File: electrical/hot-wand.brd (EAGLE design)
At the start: 112 x 72 mm, 192 parts, among them IC1 12V R-78K12-2.0, IC2 3V3 R-78K3.3, Q1 STP19NF20, Q2 IRF510, Q3 BC846B, Q4 SIS862ADN-T1-GE3, Q5 2N7002K, Q6 DMTH64M2LPDWQ-13, Q7 SIS862ADN-T1-GE3, Q8 G3404, U1 TPS54560DDA, U2 1EDN8511BXUSA1, U3 INA138, U4 LM74700QDBVTQ1, U5 AP53781, U6 SSD1306-4PIN-0.91N-VERT, U7 STM32F030F4P6, Y1 27.12 MHz 10pF

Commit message: Update hot-wand.brd
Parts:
- moved LED1 19.3 mm to (24.0, 70.1), turned to 0 degrees
- moved R39 10.9 mm to (25.7, 64.8), turned to 0 degrees
- moved R38 8.33 mm to (29.0, 64.8)
- moved LED2 1.80 mm to (25.8, 43.3)
- moved C5 0.50 mm to (29.5, 61.5)
- moved R44 0.30 mm to (20.7, 16.0)
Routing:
- net N$46: track 2.35 -> 4.90 mm
- net N$47: track 4.10 -> 2.30 mm
- net N$35: track 23.8 -> 24.9 mm
- net N$44: track 20.8 -> 21.7 mm
- net GND: vias 657 -> 655

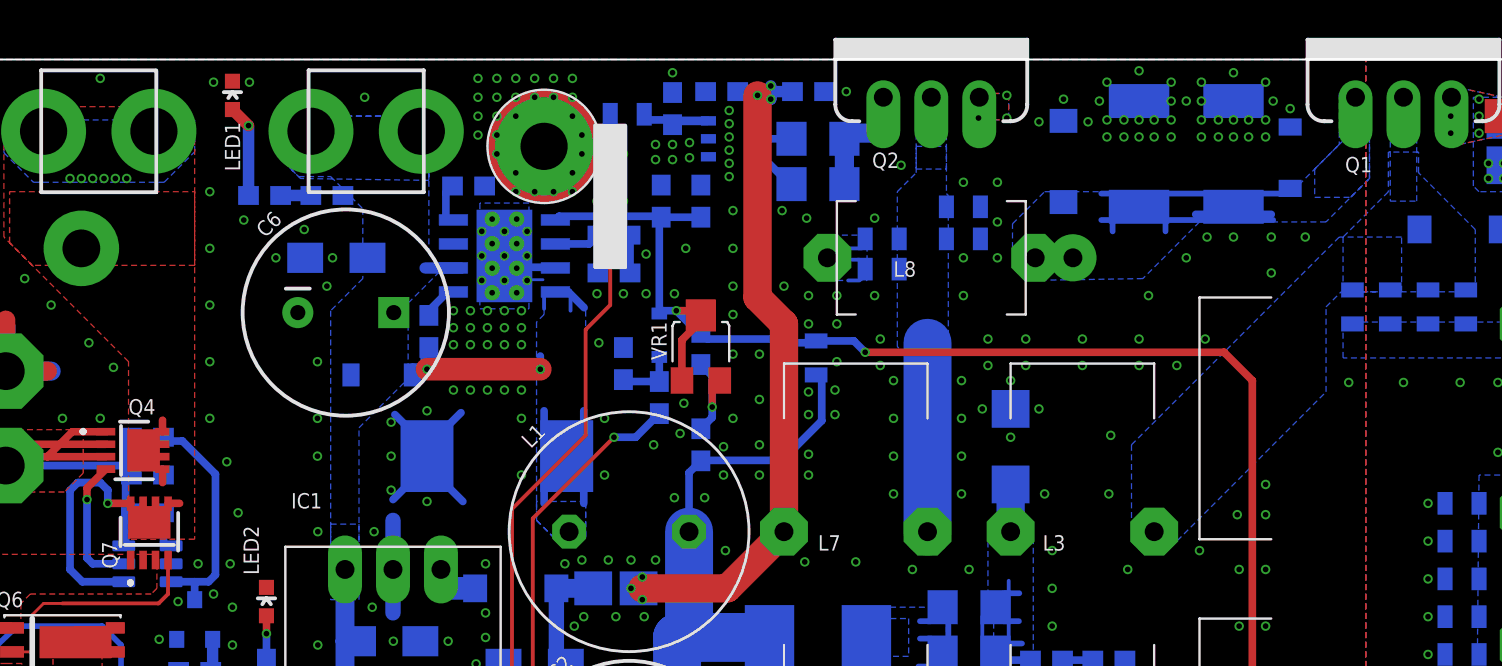
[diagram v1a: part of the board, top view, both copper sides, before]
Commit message: brd change, option for larger TH resistors over SMD ones
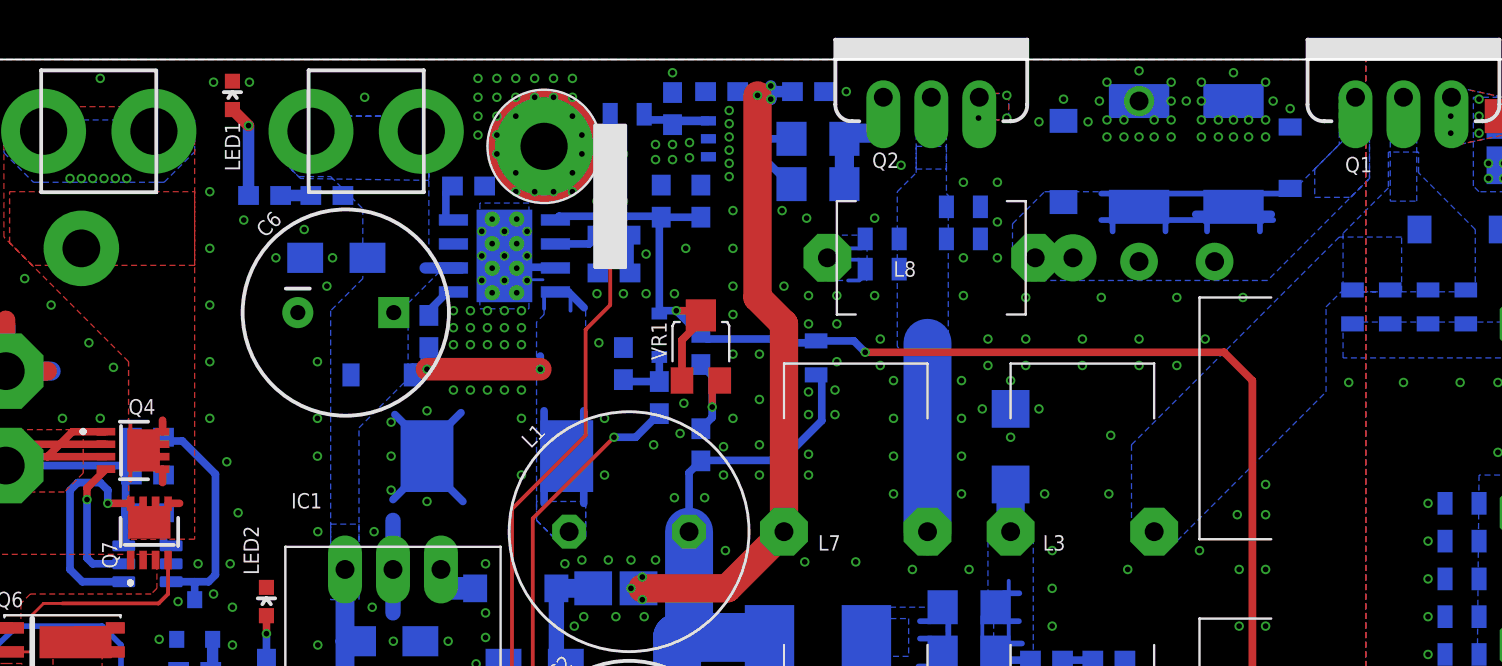
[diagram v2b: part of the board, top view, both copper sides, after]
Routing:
- net DC-SRC: track 13.5 -> 16.6 mm
- net RF-GATE: track 23.7 -> 24.7 mm, vias 1 -> 3
- net GND: vias 655 -> 652
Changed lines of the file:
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@@
 </element>
 <element name="D9" library="hot-wand" package="SOD123FL" value="STPS0540Z" x="80" y="66.8" smashed="yes" rot="MR90">
-<attribute name="NAME" x="80.316" y="69.211" size="0.8128" layer="26" font="vector" rot="MR90"/>
+<attribute name="NAME" x="80.416" y="69.311" size="0.8128" layer="26" font="vector" rot="MR90"/>
 <attribute name="JLCPARTNUM" value="C181835" x="80" y="66.8" size="1.778" layer="28" rot="MR90" display="off"/>
 </element>
 <element name="R13" library="hot-wand" package="R2512" value="DNP" x="72" y="67" smashed="yes" rot="MR270">
-<attribute name="NAME" x="70.16" y="62.795" size="0.8128" layer="26" font="vector" rot="MR180"/>
-<attribute name="VALUE" x="70.16" y="61.775" size="0.8128" layer="28" font="vector" rot="MR180"/>
+<attribute name="NAME" x="70.26" y="67.395" size="0.8128" layer="26" font="vector" rot="MR180"/>
+<attribute name="VALUE" x="70.26" y="66.375" size="0.8128" layer="28" font="vector" rot="MR180"/>
 <attribute name="PARTNUM" value="CRGP2512F150R" x="72" y="67" size="1.778" layer="28" rot="MR270" display="off"/>
 <attribute name="JLC-DNP" value="1" x="72" y="67" size="1.778" layer="28" rot="MR270" display="off"/>
 </element>
 <element name="R12" library="hot-wand" package="R2512" value="150Ω 2W" x="77" y="67" smashed="yes" rot="MR270">
-<attribute name="NAME" x="75.26" y="62.795" size="0.8128" layer="26" font="vector" rot="MR180"/>
-<attribute name="VALUE" x="74.875" y="67.64" size="0.8128" layer="28" font="vector" rot="MR270"/>
+<attribute name="NAME" x="77.16" y="62.795" size="0.8128" layer="26" font="vector" rot="MR180"/>
+<attribute name="VALUE" x="74.875" y="68.04" size="0.8128" layer="28" font="vector" rot="MR270"/>
 <attribute name="PARTNUM" value="CRGP2512F150R" x="77" y="67" size="1.778" layer="28" rot="MR270" display="off"/>
 <attribute name="JLCPARTNUM" value="C175287" x="77" y="67" size="1.778" layer="28" rot="MR270" display="off"/>
@@
 <via x="62.6" y="53" extent="1-16" drill="0.3" shape="octagon"/>
 <via x="62.6" y="55" extent="1-16" drill="0.3" shape="octagon"/>
-<via x="80.8" y="62.6" extent="1-16" drill="0.3" shape="octagon"/>
-<via x="79" y="62.6" extent="1-16" drill="0.3" shape="octagon"/>
-<via x="79" y="60.7" extent="1-16" drill="0.3" shape="octagon"/>
 <via x="80" y="69.4" extent="1-16" drill="0.3" shape="octagon"/>
 <via x="79.1" y="69.8" extent="1-16" drill="0.3" shape="octagon"/>
@@
 <via x="78.7" y="68.8" extent="1-16" drill="0.3" shape="square"/>
 <via x="75.3" y="68.8" extent="1-16" drill="0.3" shape="square"/>
-<via x="72" y="68.8" extent="1-16" drill="0.3" shape="square"/>
 <via x="77" y="68.8" extent="1-16" drill="0.3" shape="square"/>
 <via x="75.3" y="69.8" extent="1-16" drill="0.3" shape="square"/>
@@
 <via x="38.4" y="54.5" extent="1-16" drill="0.3" shape="octagon"/>
 <via x="39.3" y="54.5" extent="1-16" drill="0.3" shape="octagon"/>
-<via x="77" y="62.6" extent="1-16" drill="0.3" shape="octagon"/>
-<via x="75.6" y="62.6" extent="1-16" drill="0.3" shape="octagon"/>
-<via x="74.5" y="61.5" extent="1-16" drill="0.3" shape="octagon"/>
-<via x="72.5" y="59.5" extent="1-16" drill="0.3" shape="octagon"/>
 <via x="29" y="7.4" extent="1-16" drill="0.3" shape="octagon"/>
 <polygon width="0.2032" layer="16" spacing="0.2032" isolate="0.2032" thermals="no">
@@
 <via x="19.8" y="15" extent="1-16" drill="0.3" shape="octagon"/>
 <via x="23" y="15" extent="1-16" drill="0.3" shape="octagon"/>
+<via x="77.5" y="59.4" extent="1-16" drill="0.3" shape="octagon"/>
+<via x="74" y="59.4" extent="1-16" drill="0.3" shape="octagon"/>
+<via x="70" y="59.4" extent="1-16" drill="0.3" shape="octagon"/>
+<via x="66" y="59.4" extent="1-16" drill="0.3" shape="octagon"/>
+<via x="72" y="69.8" extent="1-16" drill="1" diameter="1.6" shape="octagon" alwaysstop="yes"/>
 </signal>
 <signal name="RF-OUT">
@@
 <polygon width="0.2032" layer="16" spacing="0.2032" isolate="0.8" rank="2">
 <vertex x="85.2" y="67.1"/>
-<vertex x="85.2" y="65"/>
-<vertex x="82.8" y="62.6"/>
+<vertex x="85.2" y="65.2"/>
+<vertex x="82.8" y="62.8"/>
 <vertex x="82.8" y="59.7"/>
 <vertex x="89.8" y="59.7"/>
@@
 <vertex x="84.2" y="67.9"/>
 <vertex x="84.2" y="65.7"/>
-<vertex x="81.9" y="63.4"/>
-<vertex x="75.2" y="63.4"/>
-<vertex x="72.2" y="60.4"/>
+<vertex x="78.8" y="60.3"/>
 <vertex x="66" y="60.3"/>
 </polygon>
@@
 <via x="68.5" y="61.5" extent="1-16" drill="1" diameter="2.5" shape="octagon" alwaysstop="yes"/>
 <wire x1="75" y1="63.8" x2="79" y2="63.8" width="0.4064" layer="16"/>
+<via x="72" y="61.3" extent="1-16" drill="1" diameter="2" shape="octagon" alwaysstop="yes"/>
+<via x="76" y="61.3" extent="1-16" drill="1" diameter="2" shape="octagon" alwaysstop="yes"/>
+<wire x1="78.4" y1="63.4" x2="78.4" y2="62.9" width="0.3048" layer="16"/>
+<wire x1="75.6" y1="63.4" x2="75.6" y2="62.9" width="0.3048" layer="16"/>
 </signal>
 <signal name="N$14">
@@
 <wire x1="20.3" y1="49.6" x2="20.3" y2="50.3" width="0.4064" layer="1"/>
 <wire x1="20.3" y1="52.9" x2="20.3" y2="52.3" width="0.4064" layer="1"/>
+<wire x1="18.6" y1="52.8" x2="18.6" y2="49.7" width="0.2032" layer="1"/>
 </signal>
 <signal name="N$27">

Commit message: no more thermal pad layer, added a bridge-able pot footprint
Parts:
- VR2, VR3: device hot-wand:TRIM_35WR1KLFTR_V2 -> hot-wand:TRIM_35WR1KLFTR_V3
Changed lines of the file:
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@@
 <wire x1="13.9" y1="37" x2="18.1" y2="37" width="0" layer="41"/>
 <wire x1="18.1" y1="37" x2="18.6" y2="37.5" width="0" layer="41"/>
-<polygon width="0.01" layer="254">
-<vertex x="13" y="58"/>
-<vertex x="13" y="65.6"/>
-<vertex x="28.3" y="65.6"/>
-<vertex x="28.3" y="60.9"/>
-<vertex x="26" y="58.6"/>
-<vertex x="26" y="55"/>
-<vertex x="32" y="55"/>
-<vertex x="32" y="48"/>
-<vertex x="28" y="48"/>
-<vertex x="28" y="45"/>
-<vertex x="23" y="45"/>
-<vertex x="23" y="48"/>
-<vertex x="22" y="48"/>
-<vertex x="22" y="53.5"/>
-<vertex x="15.6" y="53.5"/>
-<vertex x="15.6" y="58"/>
-</polygon>
-<polygon width="0.01" layer="254">
-<vertex x="36.6" y="71"/>
-<vertex x="36.6" y="66.3"/>
-<vertex x="38.4" y="66.3"/>
-<vertex x="38.4" y="64.3"/>
-<vertex x="45.2" y="64.3"/>
-<vertex x="45.2" y="71"/>
-</polygon>
-<polygon width="0.01" layer="254">
-<vertex x="35.3" y="58.8"/>
-<vertex x="35.3" y="54.4"/>
-<vertex x="43.7" y="54.4"/>
-<vertex x="43.7" y="58.8"/>
-</polygon>
-<polygon width="0.01" layer="254">
-<vertex x="43.2" y="42.6"/>
-<vertex x="50.6" y="42.6"/>
-<vertex x="50.6" y="36"/>
-<vertex x="43.2" y="36"/>
-</polygon>
-<polygon width="0.01" layer="254">
-<vertex x="76.5" y="33.8"/>
-<vertex x="69.1" y="33.8"/>
-<vertex x="69.1" y="40"/>
-<vertex x="84.1" y="55"/>
-<vertex x="87.2" y="55"/>
-<vertex x="87.2" y="18.5"/>
-<vertex x="85.280696875" y="18.5"/>
-<vertex x="82.7" y="15.919303125"/>
-<vertex x="82.7" y="9.2"/>
-<vertex x="75.5" y="9.2"/>
-<vertex x="75.5" y="12.5857875"/>
-<vertex x="74.0857875" y="14"/>
-<vertex x="73.4" y="14"/>
-<vertex x="73.4" y="24.7"/>
-<vertex x="75.1" y="24.7"/>
-<vertex x="75.1" y="28.3"/>
-<vertex x="76.5" y="28.3"/>
-</polygon>
-<polygon width="0.01" layer="254">
-<vertex x="98.8" y="12"/>
-<vertex x="98.8" y="57"/>
-<vertex x="111" y="57"/>
-<vertex x="111" y="12"/>
-</polygon>
-<polygon width="0.01" layer="254">
-<vertex x="1" y="20.4"/>
-<vertex x="18" y="20.4"/>
-<vertex x="38" y="20.4"/>
-<vertex x="38" y="8.5"/>
-<vertex x="18.6" y="8.5"/>
-<vertex x="15.3" y="11.8"/>
-<vertex x="10.1" y="11.8"/>
-<vertex x="4.3" y="6"/>
-<vertex x="1" y="6"/>
-</polygon>
-<polygon width="0.01" layer="254">
-<vertex x="46" y="62.8"/>
-<vertex x="48.9" y="62.8"/>
-<vertex x="53.9" y="62.8"/>
-<vertex x="53.9" y="58"/>
-<vertex x="49.9" y="58"/>
-<vertex x="49.9" y="58.4"/>
-<vertex x="47.4" y="58.4"/>
-<vertex x="47.4" y="59.2"/>
-<vertex x="46" y="59.2"/>
-</polygon>
-<polygon width="0.01" layer="254">
-<vertex x="3.5" y="60.8"/>
-<vertex x="9.8" y="60.8"/>
-<vertex x="9.8" y="53"/>
-<vertex x="3.5" y="53"/>
-</polygon>
-<polygon width="0.01" layer="254">
-<vertex x="67.4" y="58"/>
-<vertex x="69.1" y="58"/>
-<vertex x="73.8" y="62.7"/>
-<vertex x="80.9" y="62.7"/>
-<vertex x="70.4" y="52.2"/>
-<vertex x="67.4" y="52.2"/>
-</polygon>
 <rectangle x1="35.8" y1="20.9" x2="37.4" y2="22.3" layer="32"/>
 <rectangle x1="24.1" y1="20.9" x2="25.8" y2="22.3" layer="32"/>
@@
 <attribute name="JLC-DNP" value="1" x="48.8" y="56.7" size="1.778" layer="28" rot="MR270" display="off"/>
 </element>
-<element name="VR2" library="hot-wand" package="TRIM_35WR1KLFTR_V2" value="1K" x="67.1" y="23.5" smashed="yes">
+<element name="VR2" library="hot-wand" package="TRIM_35WR1KLFTR_V3" value="1K" x="67.1" y="23.5" smashed="yes">
 <attribute name="PARTNUM" value="TC33X-1-102E" x="67.1" y="23.5" size="1.778" layer="27" display="off"/>
 <attribute name="NAME" x="69.15" y="21.65" size="0.8128" layer="25" font="vector" rot="R180"/>
@@
 <attribute name="JLC-DNP" value="1" x="12.5" y="25.3" size="1.778" layer="28" rot="MR0" display="off"/>
 </element>
-<element name="VR3" library="hot-wand" package="TRIM_35WR1KLFTR_V2" value="1K" x="67.1" y="27.4" smashed="yes">
+<element name="VR3" library="hot-wand" package="TRIM_35WR1KLFTR_V3" value="1K" x="67.1" y="27.4" smashed="yes">
 <attribute name="PARTNUM" value="TC33X-1-102E" x="67.1" y="27.4" size="0.8128" layer="27" display="off"/>
 <attribute name="NAME" x="66.75" y="29.15" size="0.8128" layer="25"/>

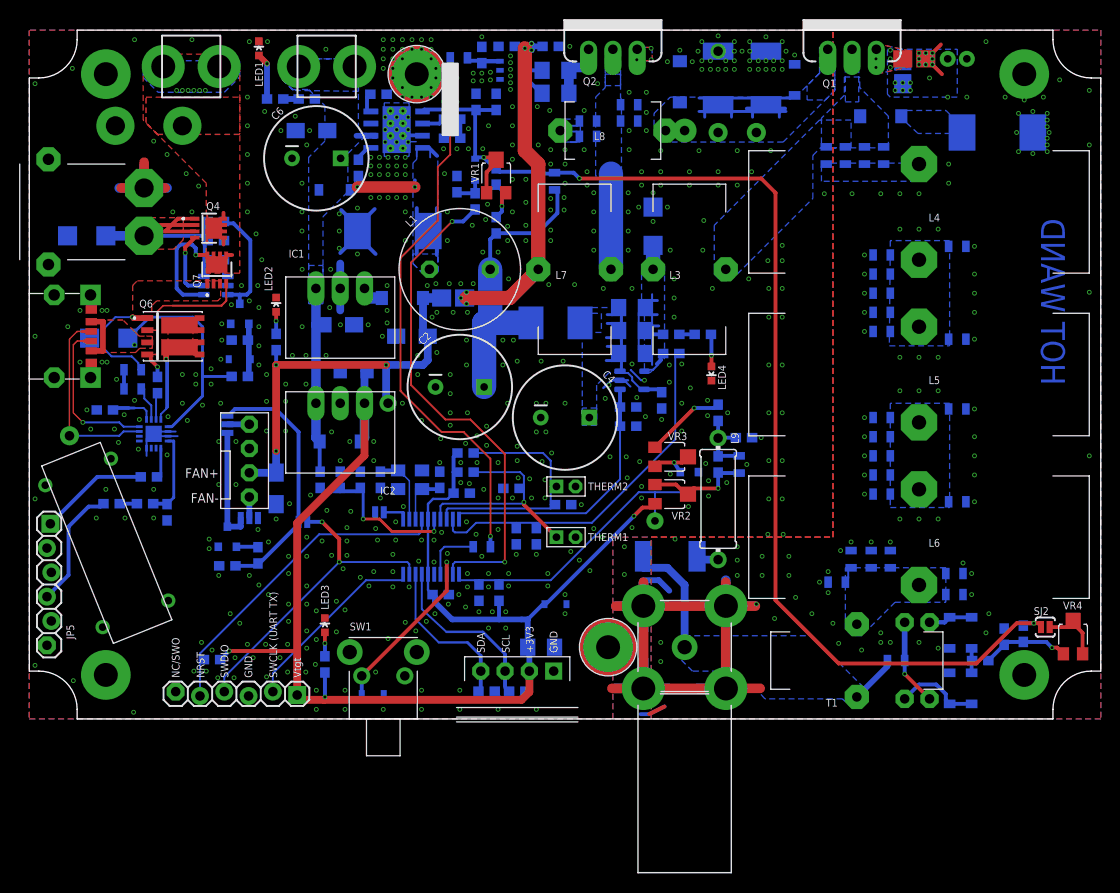
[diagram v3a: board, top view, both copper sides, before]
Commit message: significant tweaks to pcb, less DRC errors to approve
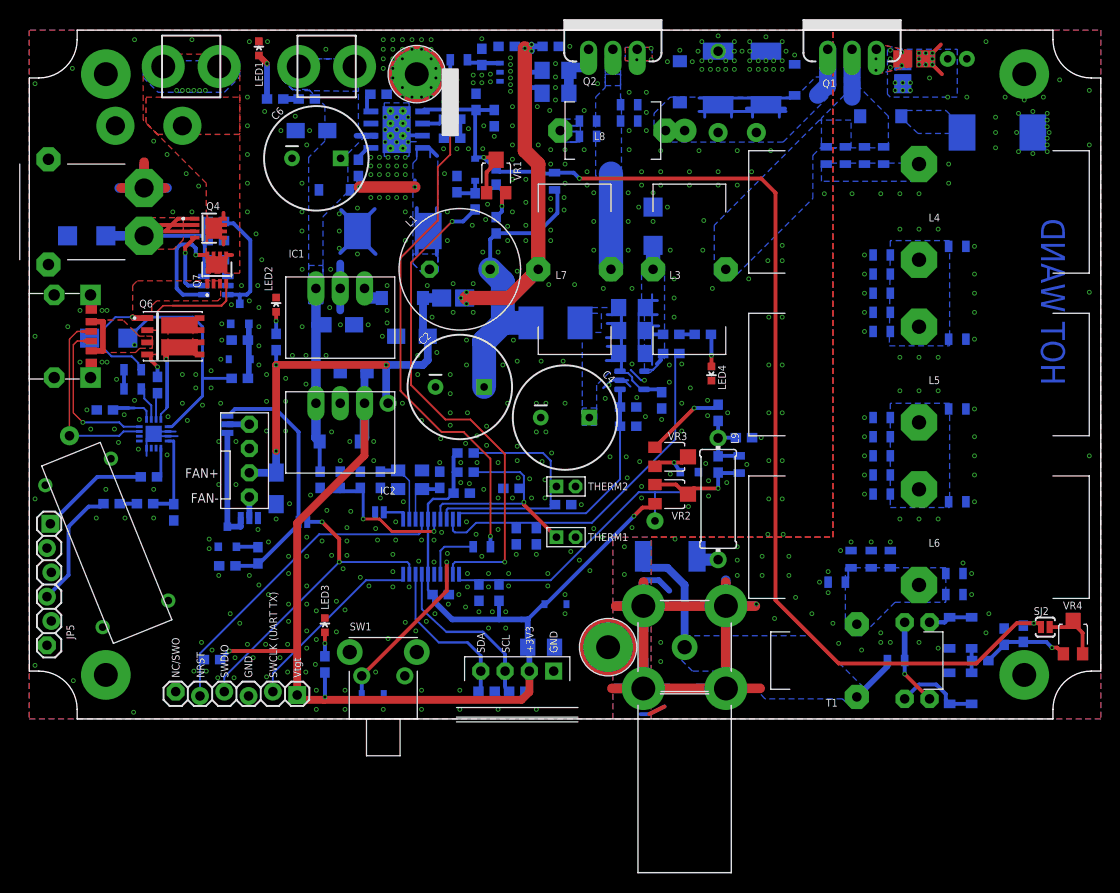
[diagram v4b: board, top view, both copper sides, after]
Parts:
- moved C8 1.71 mm to (48.6, 62.8), turned to 90 degrees
- moved R47 0.70 mm to (15.1, 21.6)
- moved R15 0.20 mm to (47.3, 69.2)
- moved U2 0.20 mm to (50.4, 67.6)
- moved R29 0.20 mm to (22.0, 35.6)
- moved R14 0.20 mm to (44.9, 68.9)
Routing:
- net RF-GATE: track 24.7 -> 29.9 mm
- net N$13: track 0.00 -> 5.00 mm
- net N$24: track 35.5 -> 30.6 mm
- net GND: vias 652 -> 651
